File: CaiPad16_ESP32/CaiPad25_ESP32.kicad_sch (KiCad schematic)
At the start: 52 parts, among them J1 OLED_128x64, U1 ESP32_DevKit_V1_DOIT

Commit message: major changes
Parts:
- removed D10, D15, D20, D21, D22, D23, D24, D25, D5: Diode, ScottoKeebs_Components:Diode_DO-35, symbol ScottoKeebs:Placeholder_Diode
- removed J1: OLED_128x64, ScottoKeebs_Components:OLED_128x64, symbol ScottoKeebs:OLED_128x64
- removed S10, S15, S20, S21, S22, S23, S24, S25, S5: Keyswitch, Button_Switch_Keyboard:SW_Cherry_MX_1.00u_PCB, symbol ScottoKeebs:Placeholder_Keyswitch
- added U2: NRF24L01_Breakout, RF_Module:nRF24L01_Breakout, symbol RF:NRF24L01_Breakout
- renumbered D12 to D10, D13 to D11, D14 to D12, D16 to D13, D17 to D14, D18 to D15, D19 to D16, D6 to D5, D7 to D6, D8 to D7, D9 to D8, D11 to D9, S12 to S10, S13 to S11, S14 to S12, S16 to S13, S17 to S14, S18 to S15, S19 to S16, S6 to S5, S7 to S6, S8 to S7, S9 to S8, S11 to S9
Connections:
- net Row 2: now also U1.21 (IO16); no longer U1.24 (IO18)
- net Row 3: now also U1.22 (IO17); no longer U1.25 (IO19)
- net GND NRF: now reaches U1.14 (GND)
- net GND NRF: now also U2.1 (GND)
- net VCC NRF: now reaches U1.16 (3V3)
- net VCC NRF: now also U2.2 (VCC)
- net CSN NRF: now reaches U1.23 (IO5)
- net CSN NRF: now also U2.4 (~{CSN})
- net MOSI NRF: now reaches U1.30 (IO23)
- net MOSI NRF: now also U2.6 (MOSI)
- net Column 4: no longer names the net of U1.13 (IO13)
- net Row 4: no longer names the net of U1.26 (IO21)
- new net MISO NRF: U1.25 (IO19), U2.7 (MISO)
- new net SCK NRF: U1.24 (IO18), U2.5 (SCK)
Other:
- moved on the sheet: U1

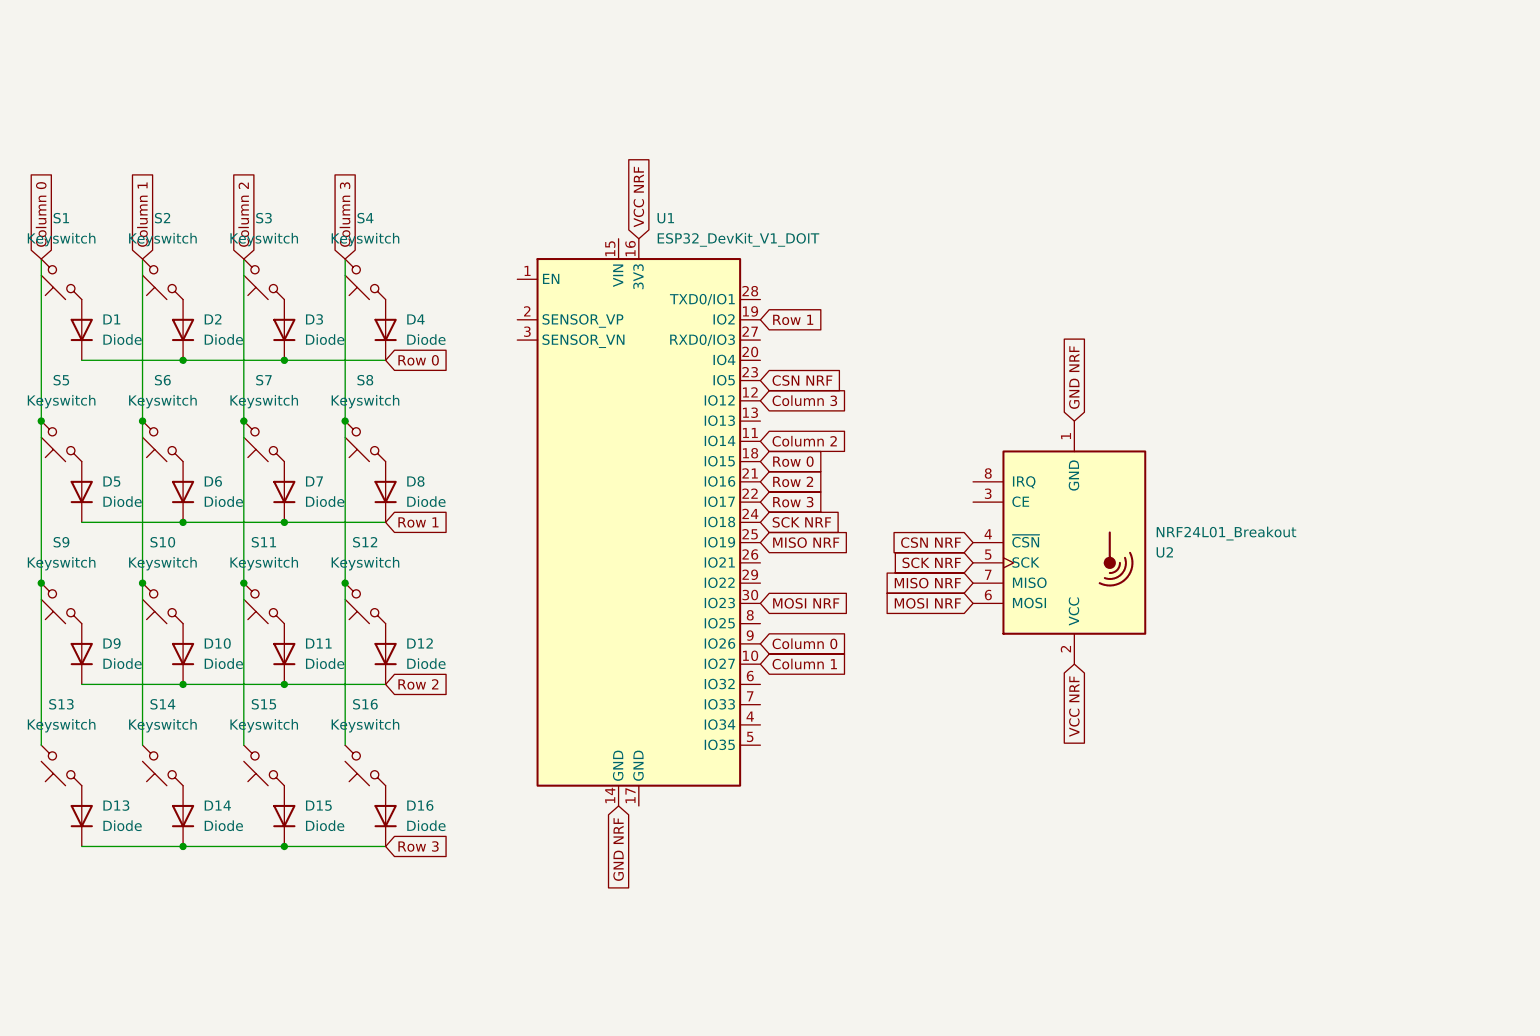
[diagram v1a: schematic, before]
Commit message: added pro micro firmware
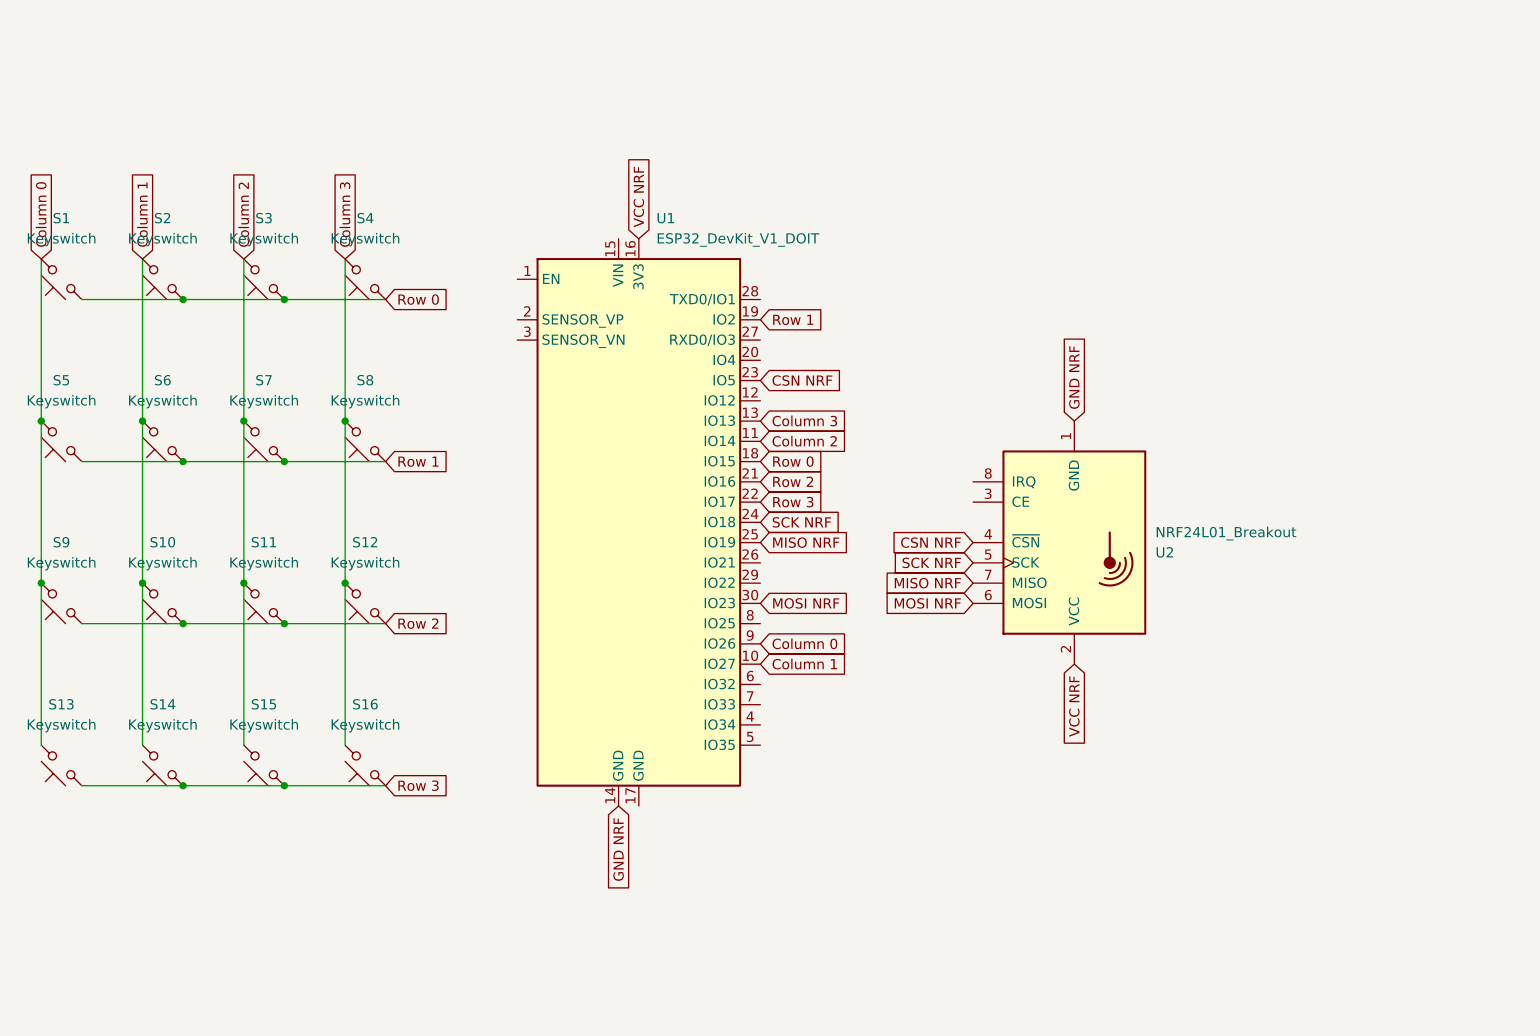
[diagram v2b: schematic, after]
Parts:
- removed D1, D10, D11, D12, D13, D14, D15, D16, D2, D3, D4, D5, D6, D7, D8, D9: Diode, ScottoKeebs_Components:Diode_DO-35, symbol ScottoKeebs:Placeholder_Diode
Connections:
- net Column 3: now also U1.13 (IO13); no longer U1.12 (IO12)
- net Row 0: now also S1.1, S2.1, S3.1, S4.1
- net Row 1: now also S5.1, S6.1, S7.1, S8.1
- net Row 2: now also S10.1, S11.1, S12.1, S9.1
- net Row 3: now also S13.1, S14.1, S15.1, S16.1
